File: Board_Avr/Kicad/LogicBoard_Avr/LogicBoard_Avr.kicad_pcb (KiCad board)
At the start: 4 copper layers, 89.2 x 87.8 mm, 50 parts, among them J1 I2C_Interface, J10 PSU Connector, J11 TriggeredStatusLedConnector, J12 PowerStatusLedConnector, J2 UART_Interface, J3 Mechanical user interface mai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, J4 Power board connector, J5 SPI Connector, J6 ICSP Header, J9 GPIO Connector, SW1 Reset switch, U1 ATmega328PB-A, U2 TLP291, U3 TLV1117-33IDCYRG3, U4 LM1117-5.0, X1 ASV-12.000MHZ-EJ-T, Y1 ABLS-20.000MHz-16-A-4-H-T

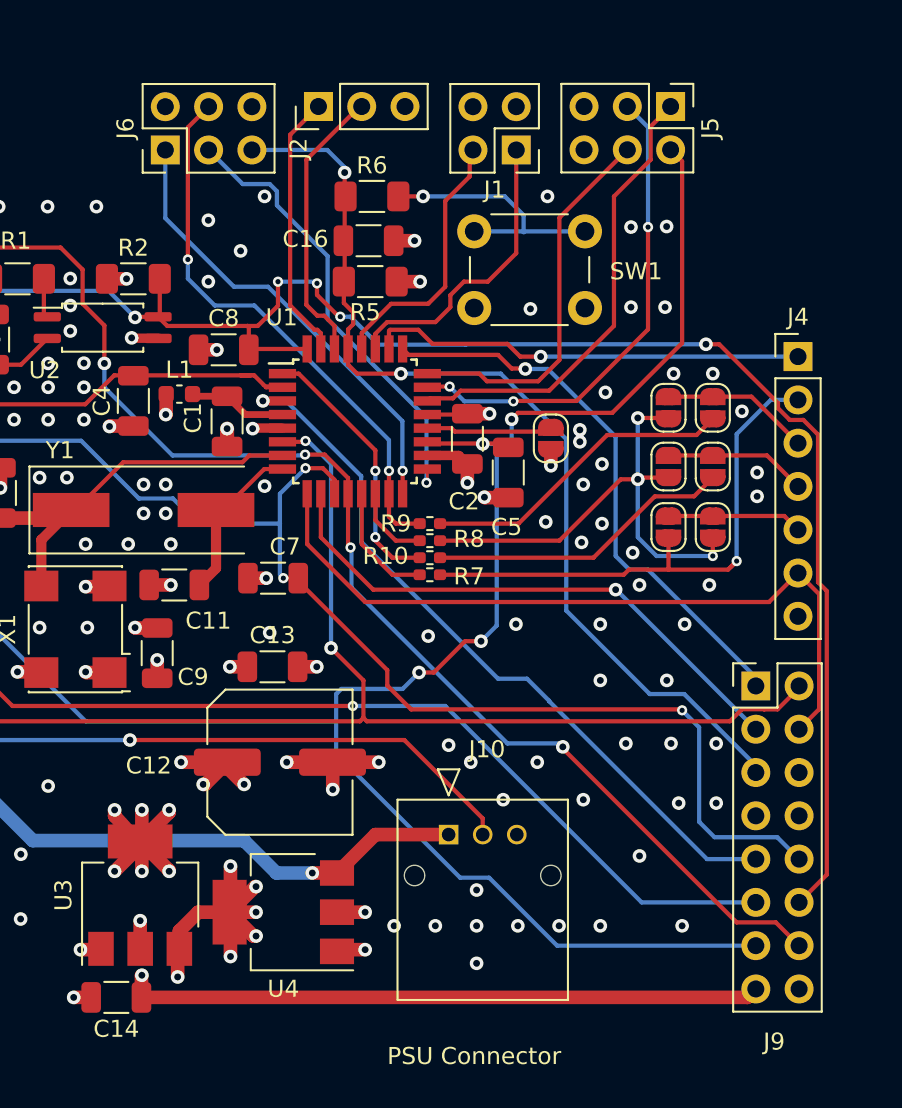
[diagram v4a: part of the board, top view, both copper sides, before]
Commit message: Cleaned last remaining track bits
Signed-off-by: bebenlebricolo <benoittarrade@hotmail.fr>
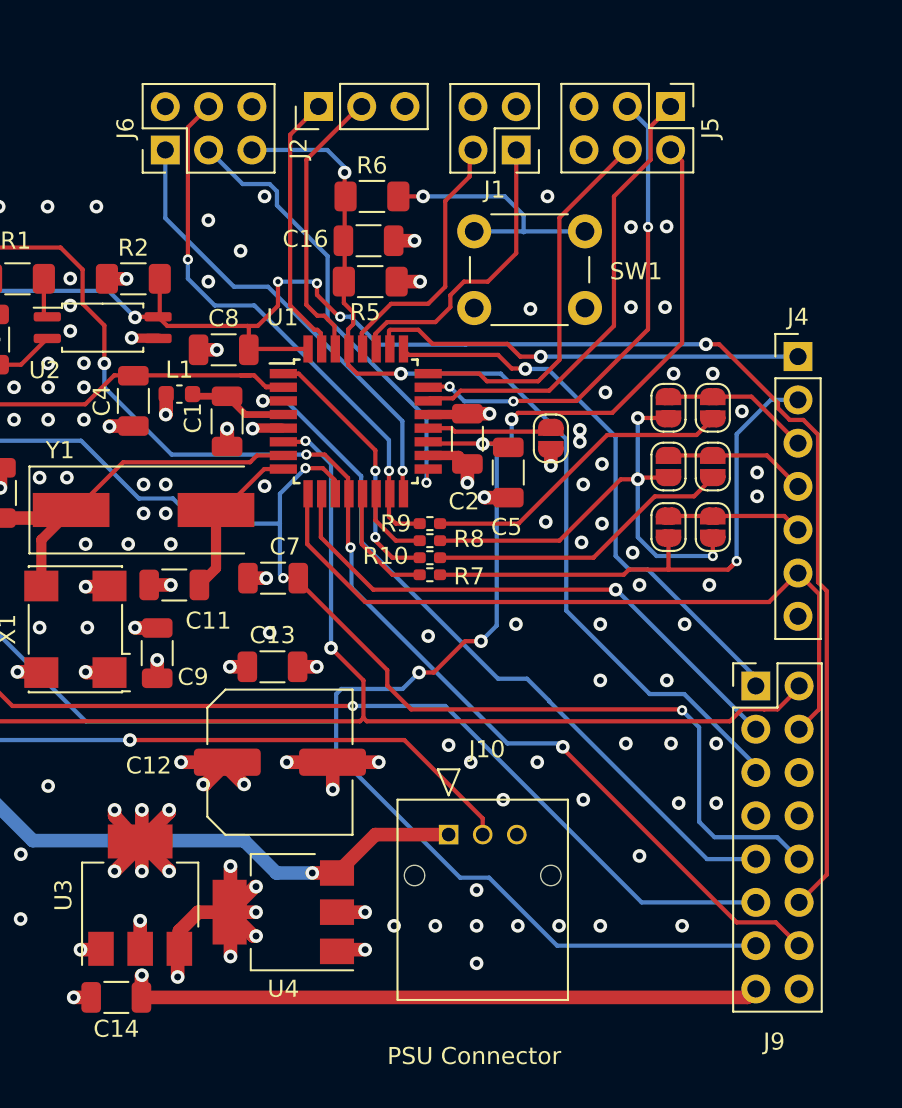
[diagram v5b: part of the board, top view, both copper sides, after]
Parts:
- moved U1 0.05 mm to (150.1, 90.0)
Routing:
- net /PowerBoardLink/OC1A_PWM_OUT: track 33.4 -> 32.0 mm
- net /PowerBoardLink/HBridgeALO: track 9.49 -> 8.68 mm
- net /PowerBoardLink/HBridgeBHO: track 9.00 -> 8.35 mm
- net /SCK0(Prog): track 27.1 -> 26.6 mm

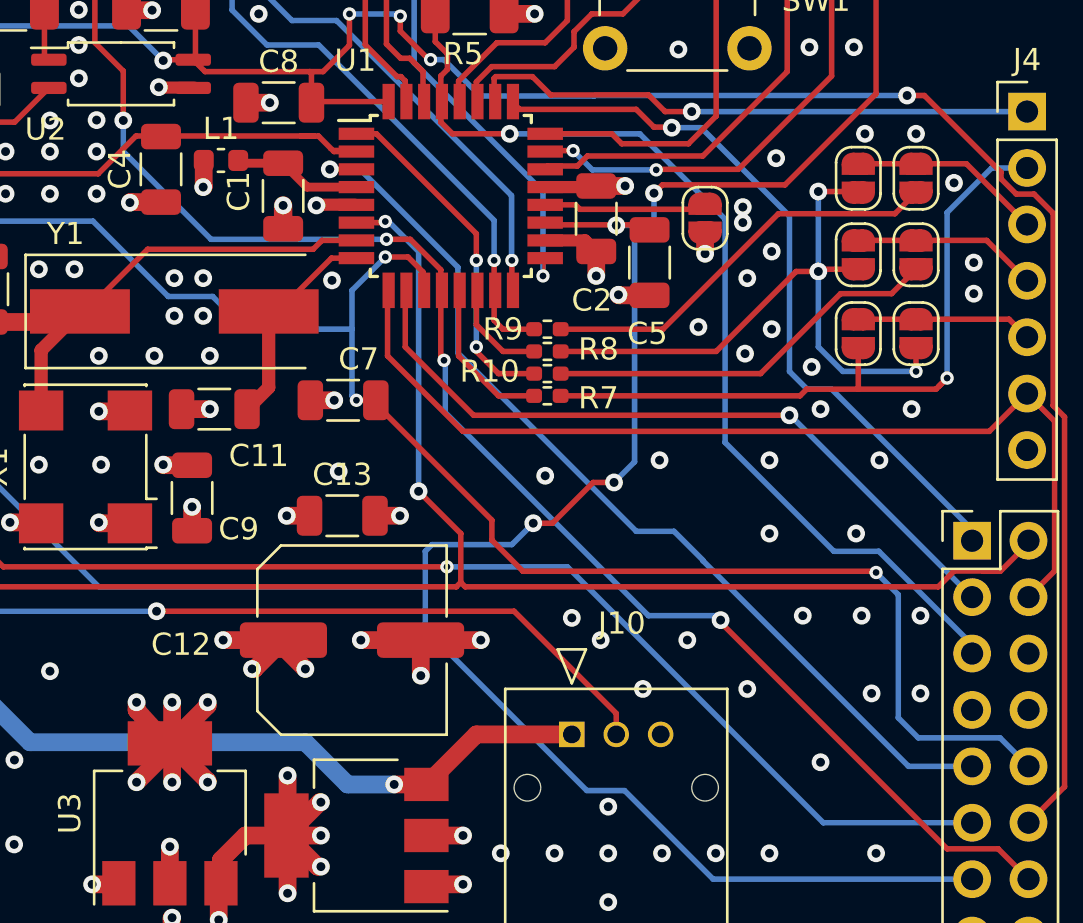
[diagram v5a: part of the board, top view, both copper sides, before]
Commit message: Same using the automatic cleanup tracks and via tool
Signed-off-by: bebenlebricolo <benoittarrade@hotmail.fr>
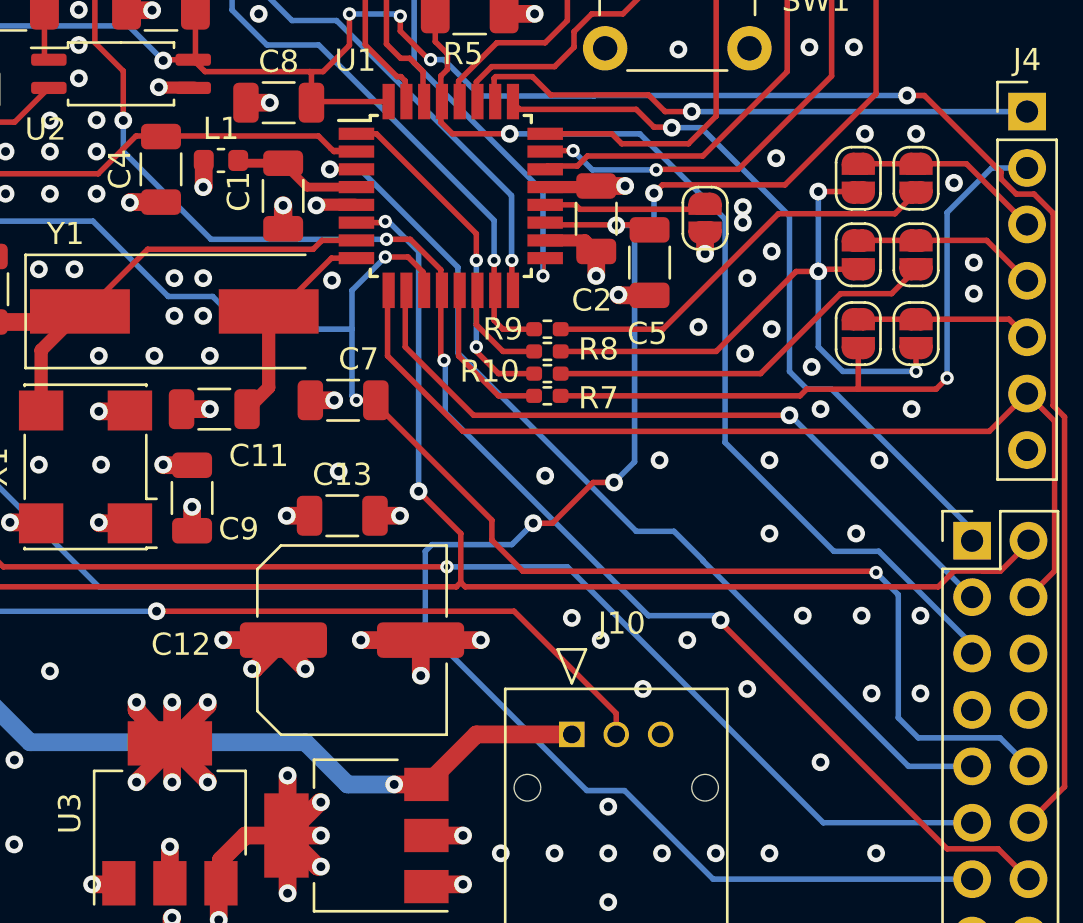
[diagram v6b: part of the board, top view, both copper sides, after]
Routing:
- net /RotEncA(In): track 93.0 -> 92.4 mm
- net /PowerBoardLink/OC1A_PWM_OUT: track 32.0 -> 31.5 mm
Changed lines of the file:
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@@
   (segment (start 135.9 113.15) (end 137.4 114.8) (width 0.8) (layer "F.Cu") (net 5))
   (segment (start 137.5 112.8) (end 137.5 114.55) (width 0.8) (layer "F.Cu") (net 5))
-  (segment (start 137.5 114.55) (end 137.4 114.65) (width 0.8) (layer "F.Cu") (net 5))
   (segment (start 137.5 122.5) (end 137.475 122.525) (width 0.8) (layer "F.Cu") (net 5))
   (segment (start 131.56 104.7) (end 131.6 104.74) (width 0.8) (layer "F.Cu") (net 5))
@@
   (segment (start 134.24 104.74) (end 135.6 104.74) (width 0.8) (layer "F.Cu") (net 5))
   (segment (start 139.1 116.4) (end 139.1 116.35) (width 0.8) (layer "F.Cu") (net 5))
-  (segment (start 139.1 116.35) (end 137.4 114.65) (width 0.8) (layer "F.Cu") (net 5))
+  (segment (start 137.4 114.65) (end 139.1 116.35) (width 0.8) (layer "F.Cu") (net 5))
   (segment (start 137.4 114.65) (end 137.4 114.9) (width 0.8) (layer "F.Cu") (net 5))
   (segment (start 138.4 104) (end 138.4 105.075) (width 0.8) (layer "F.Cu") (net 5))
-  (segment (start 139.1 112.95) (end 137.4 114.65) (width 0.8) (layer "F.Cu") (net 5))
+  (segment (start 137.4 114.65) (end 139.1 112.95) (width 0.8) (layer "F.Cu") (net 5))
   (segment (start 137.4 114.9) (end 135.9 116.4) (width 0.8) (layer "F.Cu") (net 5))
   (segment (start 137.4 119.3) (end 137.4 120.95) (width 0.8) (layer "F.Cu") (net 5))
   (segment (start 137.475 123.8) (end 173.03 123.8) (width 0.8) (layer "F.Cu") (net 5))
-  (segment (start 137.4 114.8) (end 137.4 114.65) (width 0.8) (layer "F.Cu") (net 5))
   (segment (start 139.1 112.8) (end 139.1 112.95) (width 0.8) (layer "F.Cu") (net 5))
-  (segment (start 137.5 114.75) (end 137.4 114.65) (width 0.8) (layer "F.Cu") (net 5))
   (via (at 134.2 104.7) (size 0.8) (drill 0.4) (layers "F.Cu" "B.Cu") (net 5))
   (via (at 137.5 116.4) (size 0.8) (drill 0.4) (layers "F.Cu" "B.Cu") (net 5))
@@
   (segment (start 147.101379 92.748543) (end 145.6 94.249922) (width 0.25) (layer "B.Cu") (net 32))
   (segment (start 139.325489 94.525489) (end 137.325489 94.525489) (width 0.25) (layer "B.Cu") (net 32))
-  (segment (start 143.3 87.3) (end 143.9 87.3) (width 0.25) (layer "F.Cu") (net 33))
+  (segment (start 135.874634 87.3) (end 144.089655 87.3) (width 0.25) (layer "F.Cu") (net 33))
   (segment (start 129.9 106.7) (end 149.8755 106.7) (width 0.25) (layer "F.Cu") (net 33))
   (segment (start 145.650497 87.900497) (end 145.75 88) (width 0.15) (layer "F.Cu") (net 33))
   (segment (start 134.174634 89) (end 135.874634 87.3) (width 0.25) (layer "F.Cu") (net 33))
-  (segment (start 143.3 87.3) (end 144.089655 87.3) (width 0.25) (layer "F.Cu") (net 33))
   (segment (start 126.599511 92.500489) (end 126.6 92.500978) (width 0.25) (layer "F.Cu") (net 33))
   (segment (start 126.599511 91.400489) (end 129 89) (width 0.25) (layer "F.Cu") (net 33))
   (segment (start 129 89) (end 134.174634 89) (width 0.25) (layer "F.Cu") (net 33))
   (segment (start 144.6 87.900497) (end 145.650497 87.900497) (width 0.15) (layer "F.Cu") (net 33))
-  (segment (start 135.874634 87.3) (end 143.3 87.3) (width 0.25) (layer "F.Cu") (net 33))
   (segment (start 123.299511 92.500489) (end 126.599511 92.500489) (width 0.25) (layer "F.Cu") (net 33))
   (segment (start 122.125 93.675) (end 123.299511 92.500489) (width 0.25) (layer "F.Cu") (net 33))
@@
   (segment (start 124.25 111.95) (end 124.25 115.2) (width 0.25) (layer "F.Cu") (net 43))
   (segment (start 124.2 111.9) (end 124.25 111.95) (width 0.25) (layer "F.Cu") (net 43))
-  (segment (start 172.4 98.2) (end 172.025489 98.574511) (width 0.25) (layer "F.Cu") (net 44))
   (segment (start 171.9 98.7) (end 172.4 98.2) (width 0.25) (layer "F.Cu") (net 44))
   (segment (start 165.775386 99) (end 166.075386 98.7) (width 0.25) (layer "F.Cu") (net 44))

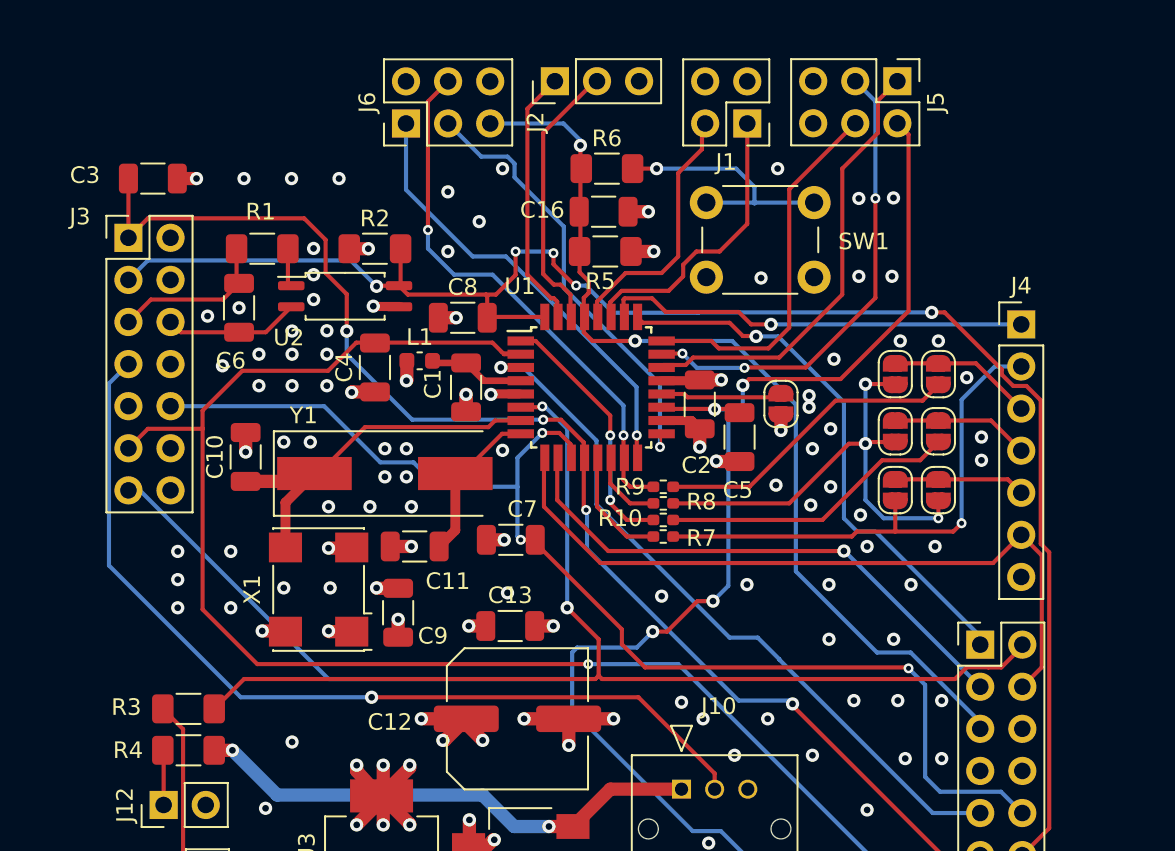
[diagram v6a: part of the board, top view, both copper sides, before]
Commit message: Fixed silkscreen and added PWM signal test points
Signed-off-by: bebenlebricolo <benoittarrade@hotmail.fr>
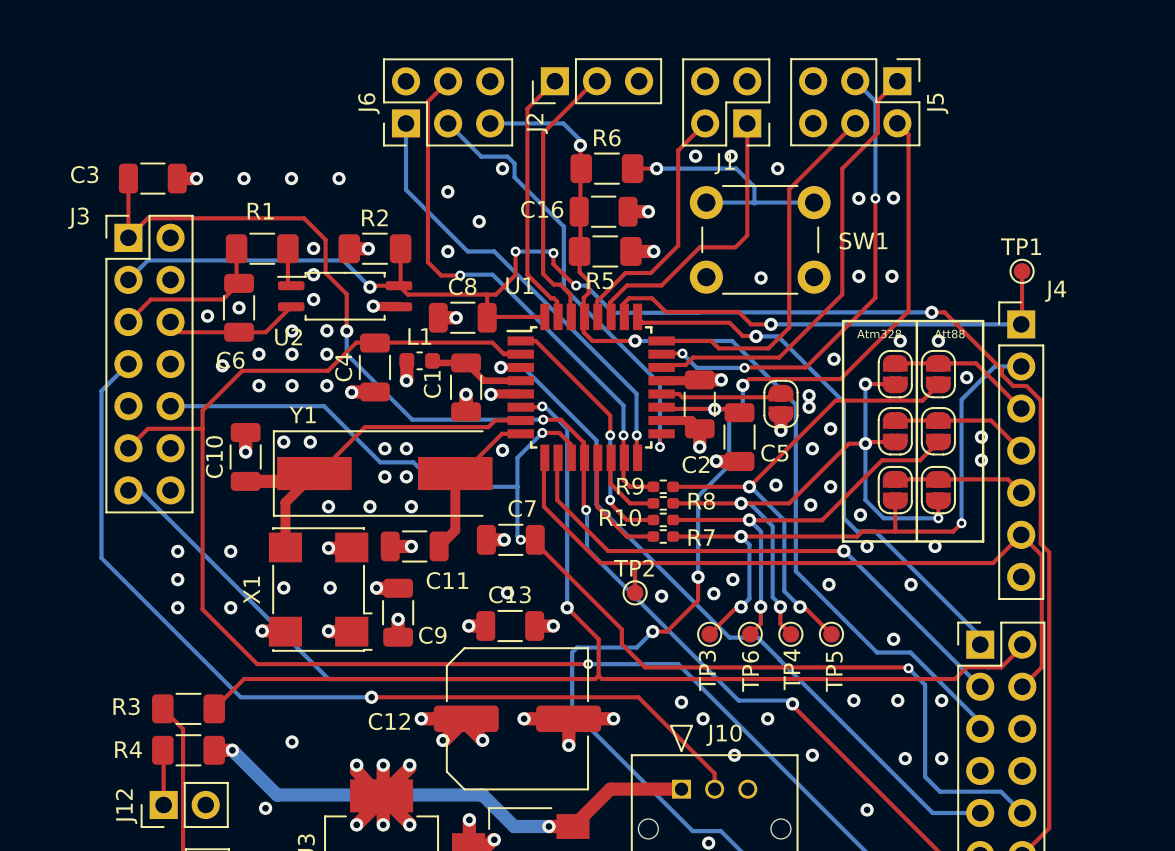
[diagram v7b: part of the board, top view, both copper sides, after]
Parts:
- added TP1: TestPoint, TestPoint:TestPoint_Pad_D1.0mm, F.Cu at (176.1, 83.0)
- added TP2: TestPoint, TestPoint:TestPoint_Pad_D1.0mm, F.Cu at (152.7, 102.4)
- added TP3: TestPoint, TestPoint:TestPoint_Pad_D1.0mm, F.Cu at (157.2, 104.9)
- added TP4: TestPoint, TestPoint:TestPoint_Pad_D1.0mm, F.Cu at (162.1, 104.9)
- added TP5: TestPoint, TestPoint:TestPoint_Pad_D1.0mm, F.Cu at (164.6, 104.9)
- added TP6: TestPoint, TestPoint:TestPoint_Pad_D1.0mm, F.Cu at (159.7, 104.9)
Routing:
- net /PowerBoardLink/OC2A_PWM_OUT: track 18.5 -> 29.7 mm, vias 0 -> 2
- net /PowerBoardLink/OC1B_PWM_OUT: track 29.7 -> 39.2 mm, vias 3 -> 5
- net /PowerBoardLink/OC2B_PWM_OUT: track 17.9 -> 25.4 mm, vias 0 -> 2
- net /PowerBoardLink/OC1A_PWM_OUT: track 31.5 -> 38.7 mm, vias 1 -> 3
- net /Ampmeter(In): track 25.7 -> 28.8 mm
- net /CoolingFan(Out): track 44.0 -> 45.8 mm
- net /IntensityPot(In): track 117.3 -> 116.7 mm
- net /OC2A_PWM: track 32.8 -> 33.3 mm
- net GND: vias 111 -> 113
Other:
- board text added: "Atm328"
- board text added: "Att88"
